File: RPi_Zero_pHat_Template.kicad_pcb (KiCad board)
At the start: 2 copper layers, 65 x 30.5 mm, 6 parts, among them J1 RPi_GPIO, J2 RPi_GPIO

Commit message: Updated to KiCad 5.0.0. Added 3d models.
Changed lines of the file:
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@@
-(kicad_pcb (version 4) (host pcbnew 4.0.5)
+(kicad_pcb (version 20171130) (host pcbnew "(5.0.0-3-g0214c9d)")
   (general
-    (links 0)
-    (no_connects 0)
-    (area 1.450001 7.175 93.121429 60.381101)
     (thickness 1.6)
     (drawings 20)
@@
       (layerselection 0x01330_80000001)
       (usegerberextensions false)
+      (usegerberattributes false)
+      (usegerberadvancedattributes false)
+      (creategerberjobfile false)
       (excludeedgelayer true)
       (linewidth 0.100000)
@@
       (hpglpennumber 1)
       (hpglpenspeed 20)
-      (hpglpendiameter 15)
-      (hpglpenoverlay 2)
+      (hpglpendiameter 15.000000)
       (psnegative false)
       (psa4output false)
@@
       (drillshape 2)
       (scaleselection 1)
-      (outputdirectory meta/))
+      (outputdirectory "meta/"))
   )
   (net 0 "")
@@
     (descr "Through hole pin header")
     (tags "pin header")
-    (fp_text reference J2 (at -5 -21 360) (layer F.SilkS)
-      (effects (font (size 1 1) (thickness 0.15)))
-    )
-    (fp_text value RPi_GPIO (at -1.27 -27.23 90) (layer F.Fab) hide
+    (fp_text reference J2 (at -5.02 -24) (layer F.SilkS)
+      (effects (font (size 1 1) (thickness 0.15)))
+    )
+    (fp_text value RPi_GPIO (at -5.08 0 180) (layer F.Fab) hide
       (effects (font (size 1 1) (thickness 0.15)))
     )
@@
     (pad 40 thru_hole oval (at 1.27 24.13 90) (size 1.7272 1.7272) (drill 1.016) (layers *.Cu *.Mask F.SilkS)
       (net 80 "Net-(J2-Pad40)"))
-    (model Pin_Headers.3dshapes/Pin_Header_Straight_2x20.wrl
-      (at (xyz 0 0 0))
+    (model ${KISYS3DMOD}/Connector_PinHeader_2.54mm.3dshapes/PinHeader_2x20_P2.54mm_Vertical.wrl
+      (offset (xyz -1.269999980926514 24.12999963760376 0))
       (scale (xyz 1 1 1))
-      (rotate (xyz 0 0 90))
+      (rotate (xyz 0 0 0))
     )
   )
   (module RPi_Hat:Samtec_HLE-120-02-XXX-DV-BE-XX-XX locked (layer F.Cu)
     (at 45 28 90)
-    (fp_text reference J1 (at -5 -24 180) (layer F.SilkS)
+    (fp_text reference J1 (at 5.14 -24 180) (layer F.SilkS)
       (effects (font (size 1 1) (thickness 0.15)))
     )
@@
     (pad "" np_thru_hole circle (at 0 -22.86) (size 1.778 1.778) (drill 1.778) (layers *.Cu *.Mask F.SilkS))
     (pad "" np_thru_hole circle (at 0 22.86) (size 1.778 1.778) (drill 1.778) (layers *.Cu *.Mask F.SilkS))
+    (model ${KIPRJMOD}/packages3d/HLE-120-02-G-DV-BE.stp
+      (at (xyz 0 0 0))
+      (scale (xyz 1 1 1))
+      (rotate (xyz -90 0 -90))
+    )
   )
   (module RPi_Hat:RPi_Hat_Mounting_Hole locked (layer F.Cu)
@@
       (solder_mask_margin 1.725) (clearance 1.725))
   )
+  (gr_arc (start 15.5 27.5) (end 12.5 27.5) (angle 90) (layer Edge.Cuts) (width 0.1))
+  (gr_line (start 15.5 24.5) (end 74.5 24.5) (angle 90) (layer Edge.Cuts) (width 0.1))
+  (gr_arc (start 74.5 27.5) (end 74.5 24.5) (angle 90) (layer Edge.Cuts) (width 0.1))
   (dimension 30.5 (width 0.15) (layer Dwgs.User)
     (gr_text "30.5 mm (SMT socket)" (at 88.05 39.25 270) (layer Dwgs.User)
@@
     (effects (font (size 1.5 1.5) (thickness 0.15)) (justify left))
   )
-  (gr_arc (start 74.5 27.5) (end 74.5 24.5) (angle 90) (layer Edge.Cuts) (width 0.1))
-  (gr_line (start 15.5 24.5) (end 74.5 24.5) (angle 90) (layer Edge.Cuts) (width 0.1))
-  (gr_arc (start 15.5 27.5) (end 12.5 27.5) (angle 90) (layer Edge.Cuts) (width 0.1))
   (dimension 3.5 (width 0.15) (layer Dwgs.User)
     (gr_text "3.5 mm" (at 21 58.5) (layer Dwgs.User)

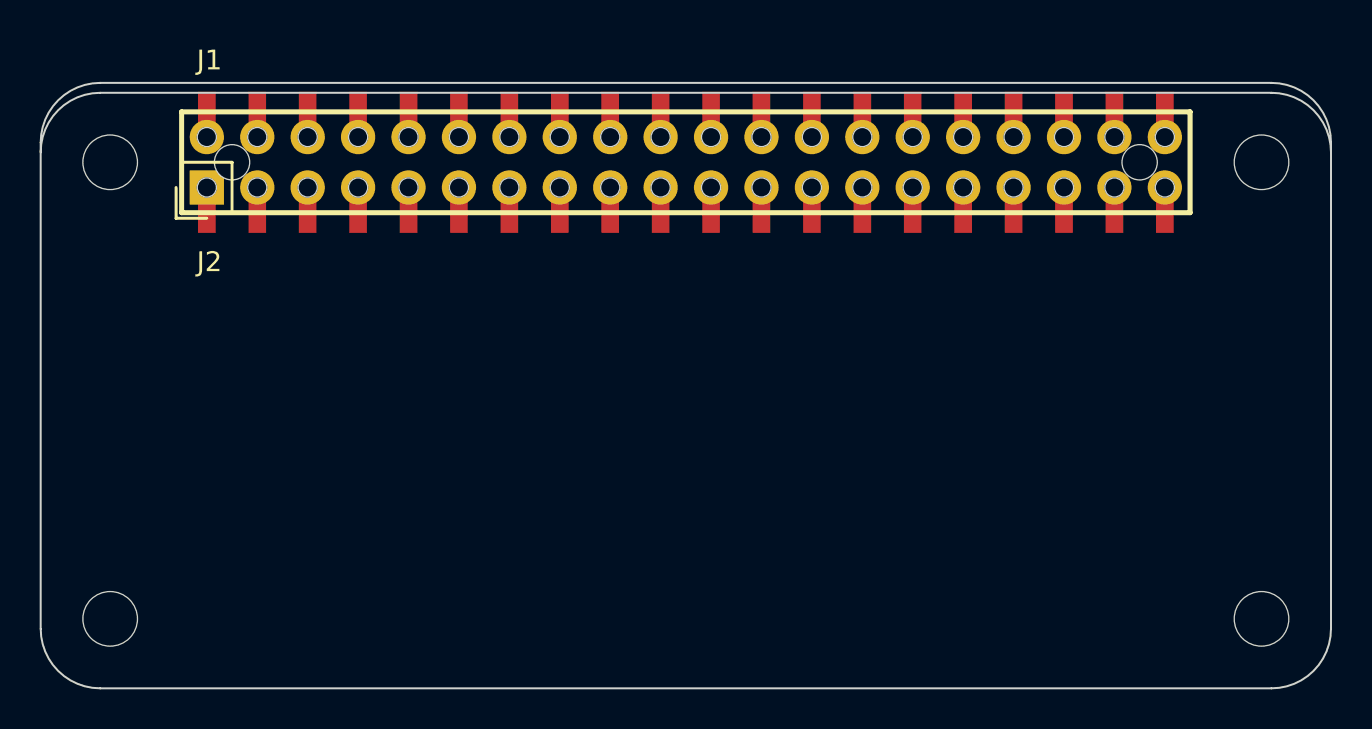
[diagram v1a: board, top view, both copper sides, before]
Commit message: Major update to KiCad 5.
Include symbol, footprints, and 3D models.
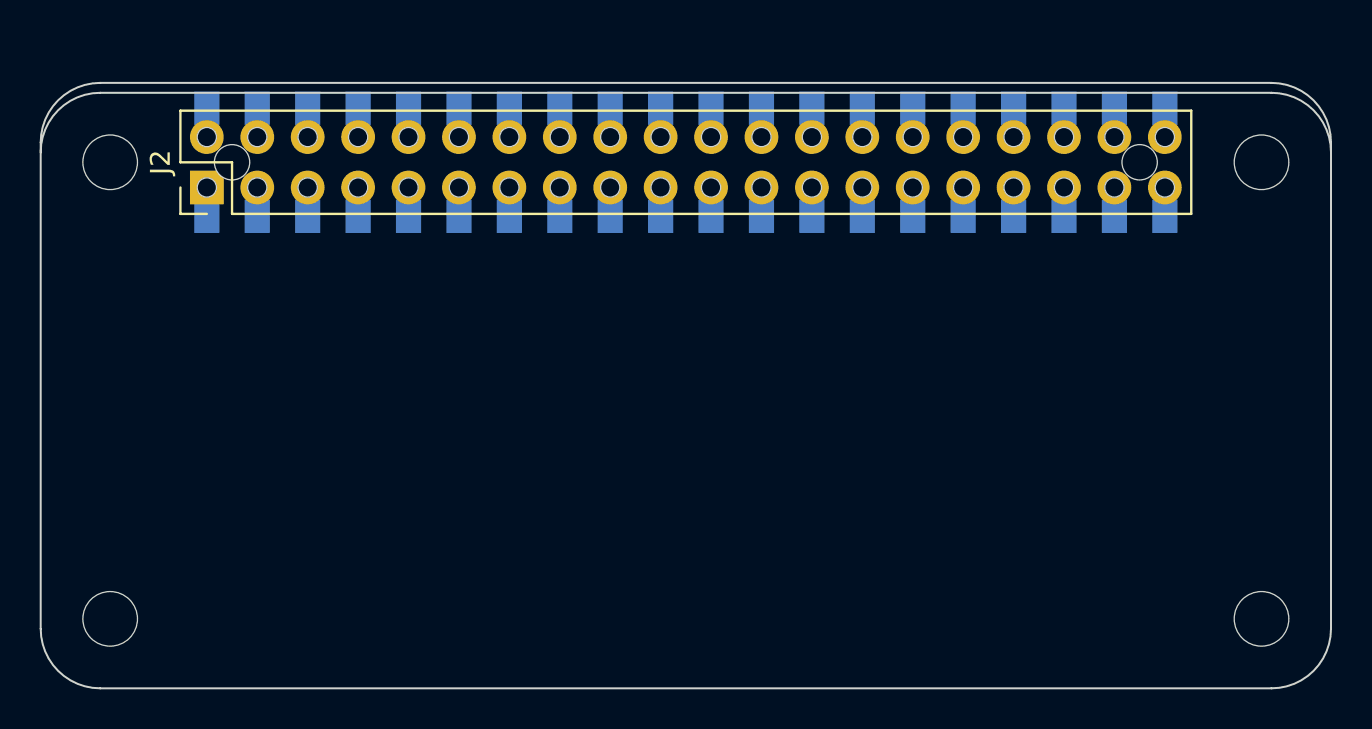
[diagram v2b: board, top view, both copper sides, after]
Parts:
- J1: footprint RPi_Hat:Samtec_HLE-120-02-XXX-DV-BE-XX-XX -> Connector_Samtec_HLE_SMD-ML:Samtec_HLE-120-02-xxx-DV-BE-A_2x20_RPi_Bottom; moved to B.Cu
- J2: footprint RPi_Hat:Pin_Header_Straight_2x20 -> Connector_PinHeader_2.54mm:PinHeader_2x20_P2.54mm_Vertical
- moved J2 24.2 mm to (20.9, 29.3)
- turned J1 to 0 degrees
